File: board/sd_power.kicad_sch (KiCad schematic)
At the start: 4 parts, among them U1201 MIC94305

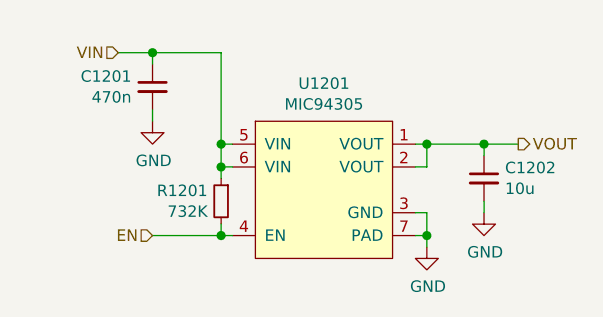
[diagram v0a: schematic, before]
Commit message: Added testpoints and other fixes
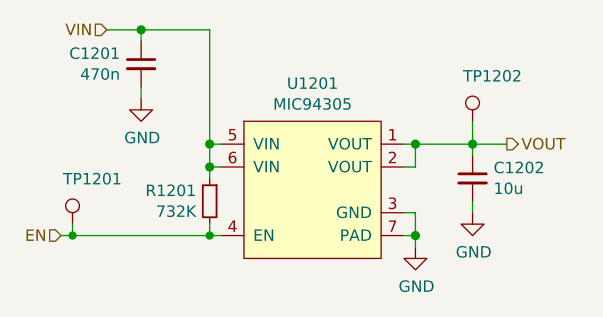
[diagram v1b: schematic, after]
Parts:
- added TP1201, TP1202: TestPoint, DIYPie:TestPoint_Pad_D1.5mm, symbol DIYPie:TestPoint
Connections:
- net EN: now also TP1201.1
- net VOUT: now also TP1202.1
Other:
- moved on the sheet: C1201, C1202, R1201, U1201
